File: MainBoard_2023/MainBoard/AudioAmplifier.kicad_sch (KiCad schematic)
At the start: 21 parts, among them J6 Conn_01x02, J7 Conn_01x02, U7 YDA142

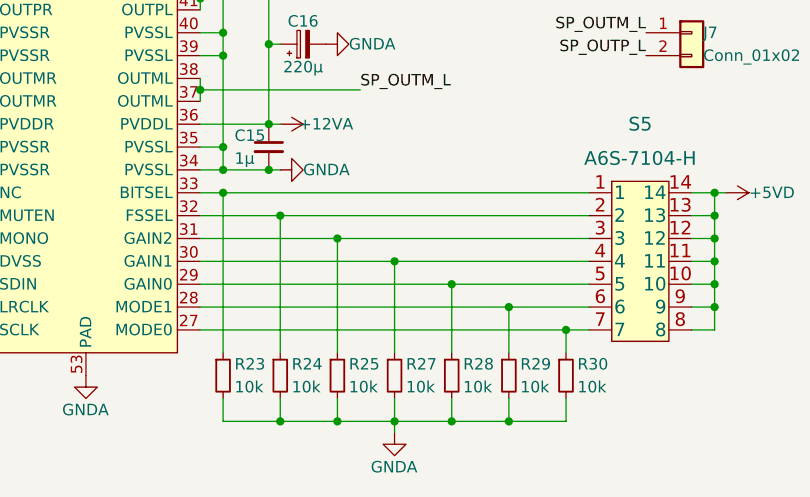
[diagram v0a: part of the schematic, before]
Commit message: アンプ周りを配線 インタラクティブルーターの設定変更
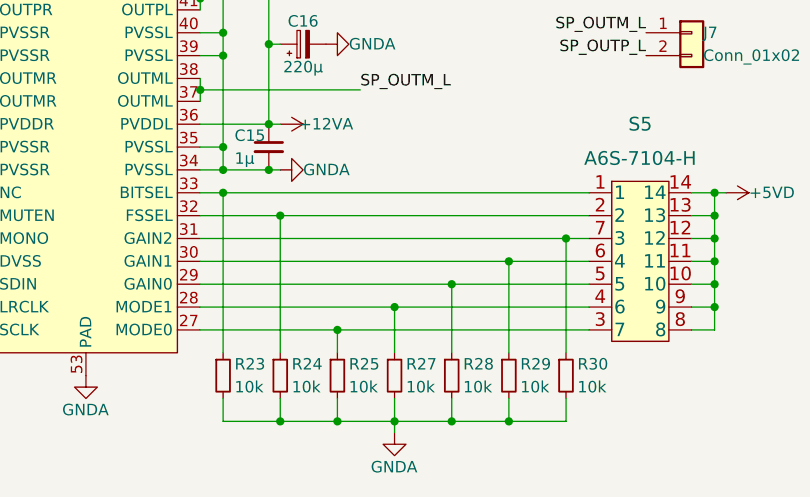
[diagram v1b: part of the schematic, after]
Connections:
- net at R29.1, S5.6 (4): now also U7.30 (GAIN1); no longer U7.28 (MODE1)
- net at R27.1, S5.4 (6): now also U7.28 (MODE1); no longer U7.30 (GAIN1)
- net at R25.1, S5.3 (7): now also U7.27 (MODE0); no longer U7.31 (GAIN2)
- net at R30.1, S5.7 (3): now also U7.31 (GAIN2); no longer U7.27 (MODE0)
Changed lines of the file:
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@@
   (junction (at 118.11 74.93) (diameter 0) (color 0 0 0 0)
   )
+  (junction (at 156.21 97.79) (diameter 0) (color 0 0 0 0)
+  )
   (junction (at 143.51 118.11) (diameter 0) (color 0 0 0 0)
   )
@@
   (junction (at 124.46 118.11) (diameter 0) (color 0 0 0 0)
   )
-  (junction (at 137.16 100.33) (diameter 0) (color 0 0 0 0)
+  (junction (at 143.51 102.87) (diameter 0) (color 0 0 0 0)
+  )
+  (junction (at 137.16 105.41) (diameter 0) (color 0 0 0 0)
   )
   (junction (at 137.16 118.11) (diameter 0) (color 0 0 0 0)
@@
   (junction (at 87.63 77.47) (diameter 0) (color 0 0 0 0)
   )
+  (junction (at 130.81 107.95) (diameter 0) (color 0 0 0 0)
+  )
   (junction (at 118.11 77.47) (diameter 0) (color 0 0 0 0)
   )
   (junction (at 123.19 85.09) (diameter 0) (color 0 0 0 0)
   )
-  (junction (at 156.21 107.95) (diameter 0) (color 0 0 0 0)
-  )
   (junction (at 172.72 102.87) (diameter 0) (color 0 0 0 0)
   )
@@
   (junction (at 123.19 90.17) (diameter 0) (color 0 0 0 0)
   )
-  (junction (at 149.86 105.41) (diameter 0) (color 0 0 0 0)
-  )
   (junction (at 128.27 62.23) (diameter 0) (color 0 0 0 0)
   )
@@
   (junction (at 118.11 87.63) (diameter 0) (color 0 0 0 0)
   )
+  (junction (at 149.86 100.33) (diameter 0) (color 0 0 0 0)
+  )
   (junction (at 87.63 49.53) (diameter 0) (color 0 0 0 0)
   )
-  (junction (at 143.51 102.87) (diameter 0) (color 0 0 0 0)
-  )
   (junction (at 87.63 90.17) (diameter 0) (color 0 0 0 0)
   )
@@
   )
   (junction (at 82.55 85.09) (diameter 0) (color 0 0 0 0)
-  )
-  (junction (at 130.81 97.79) (diameter 0) (color 0 0 0 0)
   )
   (junction (at 172.72 92.71) (diameter 0) (color 0 0 0 0)
@@
     (stroke (width 0) (type default) (color 0 0 0 0))
   )
-  (wire (pts (xy 130.81 110.49) (xy 130.81 97.79))
-    (stroke (width 0) (type default) (color 0 0 0 0))
-  )
   (wire (pts (xy 115.57 62.23) (xy 118.11 62.23))
     (stroke (width 0) (type default) (color 0 0 0 0))
@@
     (stroke (width 0) (type default) (color 0 0 0 0))
   )
-  (wire (pts (xy 137.16 110.49) (xy 137.16 100.33))
-    (stroke (width 0) (type default) (color 0 0 0 0))
-  )
   (wire (pts (xy 115.57 44.45) (xy 120.65 44.45))
     (stroke (width 0) (type default) (color 0 0 0 0))
@@
     (stroke (width 0) (type default) (color 0 0 0 0))
   )
-  (wire (pts (xy 156.21 107.95) (xy 158.75 107.95))
+  (wire (pts (xy 137.16 105.41) (xy 137.16 110.49))
     (stroke (width 0) (type default) (color 0 0 0 0))
   )
@@
     (stroke (width 0) (type default) (color 0 0 0 0))
   )
-  (wire (pts (xy 115.57 105.41) (xy 149.86 105.41))
+  (wire (pts (xy 115.57 105.41) (xy 137.16 105.41))
     (stroke (width 0) (type default) (color 0 0 0 0))
   )
@@
     (stroke (width 0) (type default) (color 0 0 0 0))
   )
+  (wire (pts (xy 156.21 97.79) (xy 156.21 110.49))
+    (stroke (width 0) (type default) (color 0 0 0 0))
+  )
   (wire (pts (xy 82.55 76.2) (xy 82.55 85.09))
     (stroke (width 0) (type default) (color 0 0 0 0))
@@
     (stroke (width 0) (type default) (color 0 0 0 0))
   )
-  (wire (pts (xy 130.81 97.79) (xy 158.75 97.79))
+  (wire (pts (xy 115.57 97.79) (xy 156.21 97.79))
     (stroke (width 0) (type default) (color 0 0 0 0))
   )
@@
     (stroke (width 0) (type default) (color 0 0 0 0))
   )
-  (wire (pts (xy 115.57 97.79) (xy 130.81 97.79))
-    (stroke (width 0) (type default) (color 0 0 0 0))
-  )
   (wire (pts (xy 172.72 97.79) (xy 172.72 100.33))
     (stroke (width 0) (type default) (color 0 0 0 0))
@@
     (stroke (width 0) (type default) (color 0 0 0 0))
   )
-  (wire (pts (xy 156.21 107.95) (xy 156.21 110.49))
+  (wire (pts (xy 130.81 107.95) (xy 130.81 110.49))
     (stroke (width 0) (type default) (color 0 0 0 0))
   )
@@
     (stroke (width 0) (type default) (color 0 0 0 0))
   )
+  (wire (pts (xy 115.57 102.87) (xy 143.51 102.87))
+    (stroke (width 0) (type default) (color 0 0 0 0))
+  )
+  (wire (pts (xy 115.57 71.12) (xy 115.57 69.85))
+    (stroke (width 0) (type default) (color 0 0 0 0))
+  )
+  (wire (pts (xy 81.28 58.42) (xy 82.55 58.42))
+    (stroke (width 0) (type default) (color 0 0 0 0))
+  )
+  (wire (pts (xy 130.81 107.95) (xy 158.75 107.95))
+    (stroke (width 0) (type default) (color 0 0 0 0))
+  )
+  (wire (pts (xy 82.55 67.31) (xy 90.17 67.31))
+    (stroke (width 0) (type default) (color 0 0 0 0))
+  )
+  (wire (pts (xy 115.57 74.93) (xy 118.11 74.93))
+    (stroke (width 0) (type default) (color 0 0 0 0))
+  )
+  (wire (pts (xy 82.55 90.17) (xy 87.63 90.17))
+    (stroke (width 0) (type default) (color 0 0 0 0))
+  )
+  (wire (pts (xy 149.86 100.33) (xy 149.86 110.49))
+    (stroke (width 0) (type default) (color 0 0 0 0))
+  )
+  (wire (pts (xy 81.28 62.23) (xy 82.55 62.23))
+    (stroke (width 0) (type default) (color 0 0 0 0))
+  )
+  (wire (pts (xy 118.11 92.71) (xy 115.57 92.71))
+    (stroke (width 0) (type default) (color 0 0 0 0))
+  )
+  (wire (pts (xy 82.55 85.09) (xy 90.17 85.09))
+    (stroke (width 0) (type default) (color 0 0 0 0))
+  )
+  (wire (pts (xy 118.11 90.17) (xy 115.57 90.17))
+    (stroke (width 0) (type default) (color 0 0 0 0))
+  )
   (wire (pts (xy 143.51 102.87) (xy 158.75 102.87))
     (stroke (width 0) (type default) (color 0 0 0 0))
   )
-  (wire (pts (xy 115.57 71.12) (xy 115.57 69.85))
-    (stroke (width 0) (type default) (color 0 0 0 0))
-  )
-  (wire (pts (xy 81.28 58.42) (xy 82.55 58.42))
-    (stroke (width 0) (type default) (color 0 0 0 0))
-  )
-  (wire (pts (xy 82.55 67.31) (xy 90.17 67.31))
-    (stroke (width 0) (type default) (color 0 0 0 0))
-  )
-  (wire (pts (xy 115.57 74.93) (xy 118.11 74.93))
-    (stroke (width 0) (type default) (color 0 0 0 0))
-  )
-  (wire (pts (xy 82.55 90.17) (xy 87.63 90.17))
-    (stroke (width 0) (type default) (color 0 0 0 0))
-  )
-  (wire (pts (xy 81.28 62.23) (xy 82.55 62.23))
-    (stroke (width 0) (type default) (color 0 0 0 0))
-  )
-  (wire (pts (xy 118.11 92.71) (xy 115.57 92.71))
-    (stroke (width 0) (type default) (color 0 0 0 0))
-  )
-  (wire (pts (xy 115.57 100.33) (xy 137.16 100.33))
-    (stroke (width 0) (type default) (color 0 0 0 0))
-  )
-  (wire (pts (xy 82.55 85.09) (xy 90.17 85.09))
-    (stroke (width 0) (type default) (color 0 0 0 0))
-  )
-  (wire (pts (xy 118.11 90.17) (xy 115.57 90.17))
-    (stroke (width 0) (type default) (color 0 0 0 0))
-  )
   (wire (pts (xy 82.55 90.17) (xy 81.28 90.17))
     (stroke (width 0) (type default) (color 0 0 0 0))
@@
     (stroke (width 0) (type default) (color 0 0 0 0))
   )
-  (wire (pts (xy 143.51 110.49) (xy 143.51 102.87))
-    (stroke (width 0) (type default) (color 0 0 0 0))
-  )
   (wire (pts (xy 118.11 77.47) (xy 118.11 87.63))
     (stroke (width 0) (type default) (color 0 0 0 0))
@@
     (stroke (width 0) (type default) (color 0 0 0 0))
   )
-  (wire (pts (xy 137.16 100.33) (xy 158.75 100.33))
+  (wire (pts (xy 115.57 100.33) (xy 149.86 100.33))
     (stroke (width 0) (type default) (color 0 0 0 0))
   )
@@
     (stroke (width 0) (type default) (color 0 0 0 0))
   )
-  (wire (pts (xy 149.86 105.41) (xy 158.75 105.41))
-    (stroke (width 0) (type default) (color 0 0 0 0))
-  )
   (wire (pts (xy 172.72 107.95) (xy 170.18 107.95))
     (stroke (width 0) (type default) (color 0 0 0 0))
@@
     (stroke (width 0) (type default) (color 0 0 0 0))
   )
+  (wire (pts (xy 149.86 100.33) (xy 158.75 100.33))
+    (stroke (width 0) (type default) (color 0 0 0 0))
+  )
   (wire (pts (xy 118.11 62.23) (xy 123.19 62.23))
     (stroke (width 0) (type default) (color 0 0 0 0))
@@
     (stroke (width 0) (type default) (color 0 0 0 0))
   )
-  (wire (pts (xy 115.57 107.95) (xy 156.21 107.95))
+  (wire (pts (xy 115.57 107.95) (xy 130.81 107.95))
     (stroke (width 0) (type default) (color 0 0 0 0))
   )
@@
     (stroke (width 0) (type default) (color 0 0 0 0))
   )
+  (wire (pts (xy 156.21 97.79) (xy 158.75 97.79))
+    (stroke (width 0) (type default) (color 0 0 0 0))
+  )
   (wire (pts (xy 118.11 92.71) (xy 158.75 92.71))
     (stroke (width 0) (type default) (color 0 0 0 0))
   )
-  (wire (pts (xy 115.57 102.87) (xy 143.51 102.87))
-    (stroke (width 0) (type default) (color 0 0 0 0))
-  )
   (wire (pts (xy 118.11 115.57) (xy 118.11 118.11))
     (stroke (width 0) (type default) (color 0 0 0 0))
@@
     (stroke (width 0) (type default) (color 0 0 0 0))
   )
+  (wire (pts (xy 143.51 102.87) (xy 143.51 110.49))
+    (stroke (width 0) (type default) (color 0 0 0 0))
+  )
   (wire (pts (xy 137.16 52.07) (xy 135.89 52.07))
     (stroke (width 0) (type default) (color 0 0 0 0))
@@
     (stroke (width 0) (type default) (color 0 0 0 0))
   )
+  (wire (pts (xy 137.16 105.41) (xy 158.75 105.41))
+    (stroke (width 0) (type default) (color 0 0 0 0))
+  )
   (wire (pts (xy 115.57 49.53) (xy 128.27 49.53))
     (stroke (width 0) (type default) (color 0 0 0 0))
   )
   (wire (pts (xy 123.19 67.31) (xy 123.19 76.2))
-    (stroke (width 0) (type default) (color 0 0 0 0))
-  )
-  (wire (pts (xy 149.86 105.41) (xy 149.86 110.49))
     (stroke (width 0) (type default) (color 0 0 0 0))
   )
@@
     (pin "14")
     (pin "2")
+    (pin "7")
+    (pin "6")
+    (pin "5")
+    (pin "4")
     (pin "3")
-    (pin "4")
-    (pin "5")
-    (pin "6")
-    (pin "7")
     (pin "8")
     (pin "9")
